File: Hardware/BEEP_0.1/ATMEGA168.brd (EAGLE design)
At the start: 48.8 x 53 mm, 22 parts, among them IC1 ATMEGA48/88/168-AU, Q1 20Mhz

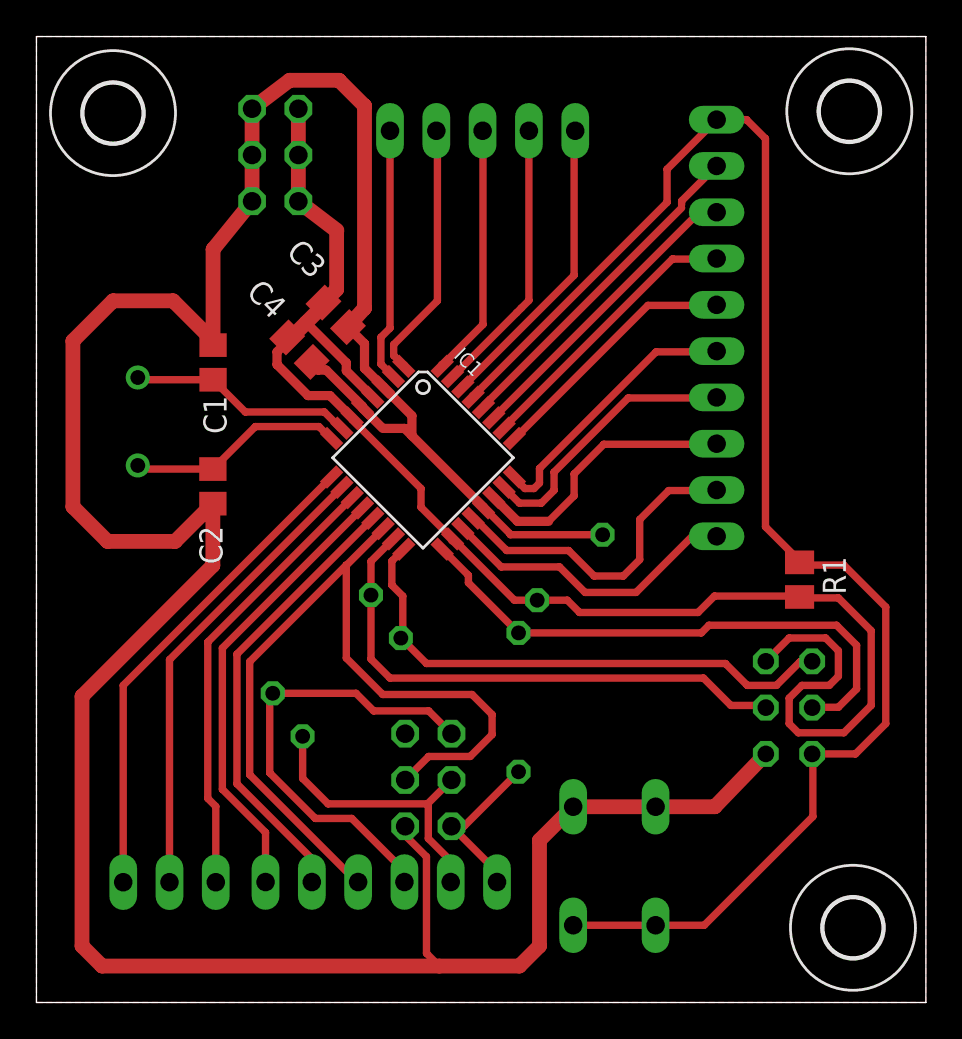
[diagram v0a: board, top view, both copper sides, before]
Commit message: enlarge Clearence to 10mil created some pdf files for the boards
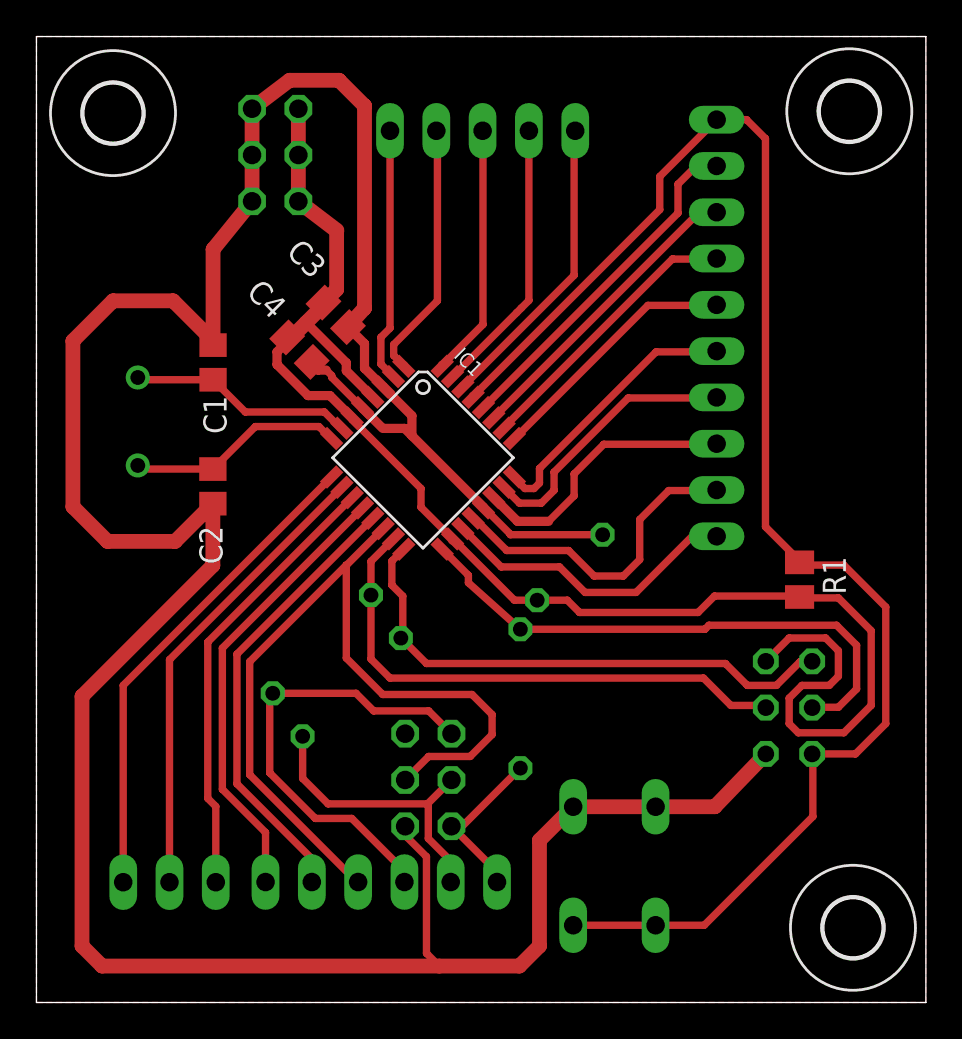
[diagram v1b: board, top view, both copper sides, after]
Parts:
- moved R4 0.22 mm to (26.6, 16.7)
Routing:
- net N$3: track 18.4 -> 19.4 mm
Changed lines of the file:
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@@
 <layers>
 <layer number="1" name="Top" color="4" fill="1" visible="yes" active="yes"/>
-<layer number="16" name="Bottom" color="1" fill="1" visible="yes" active="yes"/>
+<layer number="16" name="Bottom" color="1" fill="1" visible="no" active="yes"/>
 <layer number="17" name="Pads" color="2" fill="1" visible="yes" active="yes"/>
-<layer number="18" name="Vias" color="2" fill="1" visible="yes" active="yes"/>
-<layer number="19" name="Unrouted" color="6" fill="1" visible="yes" active="yes"/>
-<layer number="20" name="Dimension" color="15" fill="1" visible="yes" active="yes"/>
-<layer number="21" name="tPlace" color="7" fill="1" visible="yes" active="yes"/>
-<layer number="22" name="bPlace" color="7" fill="1" visible="yes" active="yes"/>
-<layer number="23" name="tOrigins" color="15" fill="1" visible="yes" active="yes"/>
-<layer number="24" name="bOrigins" color="15" fill="1" visible="yes" active="yes"/>
-<layer number="25" name="tNames" color="7" fill="1" visible="yes" active="yes"/>
-<layer number="26" name="bNames" color="7" fill="1" visible="yes" active="yes"/>
-<layer number="27" name="tValues" color="7" fill="1" visible="yes" active="yes"/>
-<layer number="28" name="bValues" color="7" fill="1" visible="yes" active="yes"/>
+<layer number="18" name="Vias" color="2" fill="1" visible="no" active="yes"/>
+<layer number="19" name="Unrouted" color="6" fill="1" visible="no" active="yes"/>
+<layer number="20" name="Dimension" color="15" fill="1" visible="no" active="yes"/>
+<layer number="21" name="tPlace" color="7" fill="1" visible="no" active="yes"/>
+<layer number="22" name="bPlace" color="7" fill="1" visible="no" active="yes"/>
+<layer number="23" name="tOrigins" color="15" fill="1" visible="no" active="yes"/>
+<layer number="24" name="bOrigins" color="15" fill="1" visible="no" active="yes"/>
+<layer number="25" name="tNames" color="7" fill="1" visible="no" active="yes"/>
+<layer number="26" name="bNames" color="7" fill="1" visible="no" active="yes"/>
+<layer number="27" name="tValues" color="7" fill="1" visible="no" active="yes"/>
+<layer number="28" name="bValues" color="7" fill="1" visible="no" active="yes"/>
 <layer number="29" name="tStop" color="7" fill="3" visible="no" active="yes"/>
 <layer number="30" name="bStop" color="7" fill="6" visible="no" active="yes"/>
@@
 <layer number="37" name="tTest" color="7" fill="1" visible="no" active="yes"/>
 <layer number="38" name="bTest" color="7" fill="1" visible="no" active="yes"/>
-<layer number="39" name="tKeepout" color="4" fill="11" visible="yes" active="yes"/>
-<layer number="40" name="bKeepout" color="1" fill="11" visible="yes" active="yes"/>
-<layer number="41" name="tRestrict" color="4" fill="10" visible="yes" active="yes"/>
-<layer number="42" name="bRestrict" color="1" fill="10" visible="yes" active="yes"/>
-<layer number="43" name="vRestrict" color="2" fill="10" visible="yes" active="yes"/>
+<layer number="39" name="tKeepout" color="4" fill="11" visible="no" active="yes"/>
+<layer number="40" name="bKeepout" color="1" fill="11" visible="no" active="yes"/>
+<layer number="41" name="tRestrict" color="4" fill="10" visible="no" active="yes"/>
+<layer number="42" name="bRestrict" color="1" fill="10" visible="no" active="yes"/>
+<layer number="43" name="vRestrict" color="2" fill="10" visible="no" active="yes"/>
 <layer number="44" name="Drills" color="7" fill="1" visible="no" active="yes"/>
-<layer number="45" name="Holes" color="7" fill="1" visible="yes" active="yes"/>
+<layer number="45" name="Holes" color="7" fill="1" visible="no" active="yes"/>
 <layer number="46" name="Milling" color="3" fill="1" visible="no" active="yes"/>
 <layer number="47" name="Measures" color="7" fill="1" visible="no" active="yes"/>
-<layer number="48" name="Document" color="7" fill="1" visible="yes" active="yes"/>
-<layer number="49" name="Reference" color="7" fill="1" visible="yes" active="yes"/>
+<layer number="48" name="Document" color="7" fill="1" visible="no" active="yes"/>
+<layer number="49" name="Reference" color="7" fill="1" visible="no" active="yes"/>
 <layer number="50" name="dxf" color="7" fill="1" visible="no" active="no"/>
-<layer number="51" name="tDocu" color="7" fill="1" visible="yes" active="yes"/>
-<layer number="52" name="bDocu" color="7" fill="1" visible="yes" active="yes"/>
+<layer number="51" name="tDocu" color="7" fill="1" visible="no" active="yes"/>
+<layer number="52" name="bDocu" color="7" fill="1" visible="no" active="yes"/>
 <layer number="91" name="Nets" color="2" fill="1" visible="no" active="no"/>
 <layer number="92" name="Busses" color="1" fill="1" visible="no" active="no"/>
@@
 </class>
 </classes>
-<designrules name="default">
+<designrules name="default *">
 <description language="de">&lt;b&gt;EAGLE Design Rules&lt;/b&gt;
 &lt;p&gt;
@@
 <param name="mtCopper" value="0.035mm 0.035mm 0.035mm 0.035mm 0.035mm 0.035mm 0.035mm 0.035mm 0.035mm 0.035mm 0.035mm 0.035mm 0.035mm 0.035mm 0.035mm 0.035mm"/>
 <param name="mtIsolate" value="1.5mm 0.15mm 0.2mm 0.15mm 0.2mm 0.15mm 0.2mm 0.15mm 0.2mm 0.15mm 0.2mm 0.15mm 0.2mm 0.15mm 0.2mm"/>
-<param name="mdWireWire" value="8mil"/>
+<param name="mdWireWire" value="10mil"/>
 <param name="mdWirePad" value="8mil"/>
 <param name="mdWireVia" value="8mil"/>
@@
 <attribute name="VALUE" x="20.911578125" y="17.5213125" size="1.27" layer="28" ratio="10" rot="MR315"/>
 </element>
-<element name="R4" library="rcl" package="0207/7" value="1k" x="26.45" y="16.47" rot="MR270"/>
+<element name="R4" library="rcl" package="0207/7" value="1k" x="26.55" y="16.67" rot="MR270"/>
 <element name="SPI" library="pinhead" package="2X03" value="" x="21.5" y="12.21" smashed="yes" rot="MR270">
 <attribute name="NAME" x="18.325" y="13.72" size="1.27" layer="26" ratio="10" rot="MR270"/>
@@
 <wire x1="18" y1="34.8" x2="18" y2="36.149996875" width="0.508" layer="1"/>
 <wire x1="18" y1="36.149996875" x2="17.09175" y2="37.058246875" width="0.508" layer="1"/>
-<wire x1="17.891828125" y1="32.64248125" x2="17.891828125" y2="32.708171875" width="0.508" layer="1"/>
-<wire x1="17.891828125" y1="32.708171875" x2="15.9" y2="34.7" width="0.508" layer="1"/>
 <wire x1="15.9" y1="34.7" x2="15.449996875" y2="34.7" width="0.508" layer="1"/>
 <wire x1="15.449996875" y1="34.7" x2="15.10175" y2="35.148246875" width="0.508" layer="1"/>
@@
 <wire x1="20.3" y1="9.1" x2="20.3" y2="9.6" width="0.4064" layer="1"/>
 <wire x1="20.3" y1="9.6" x2="20.23" y2="9.67" width="0.4064" layer="1"/>
+<wire x1="17.891828125" y1="32.64248125" x2="17.85751875" y2="32.64248125" width="0.4064" layer="1"/>
+<wire x1="17.85751875" y1="32.64248125" x2="16.2" y2="34.3" width="0.4064" layer="1"/>
+<wire x1="16.2" y1="34.3" x2="16.2" y2="34.4" width="0.4064" layer="1"/>
+<wire x1="16.2" y1="34.4" x2="15.9" y2="34.7" width="0.4064" layer="1"/>
 </signal>
 <signal name="VCC">
@@
 <wire x1="40" y1="26.1" x2="40" y2="47.4" width="0.4064" layer="1"/>
 <wire x1="40" y1="47.4" x2="38.96" y2="48.44" width="0.4064" layer="1"/>
-<wire x1="23.96248125" y1="33.26248125" x2="34.6" y2="43.9" width="0.4064" layer="1"/>
-<wire x1="34.6" y1="43.9" x2="34.6" y2="45.72" width="0.4064" layer="1"/>
-<wire x1="34.6" y1="45.72" x2="37.32" y2="48.44" width="0.4064" layer="1"/>
+<wire x1="23.96248125" y1="33.26248125" x2="34.2" y2="43.5" width="0.4064" layer="1"/>
+<wire x1="34.2" y1="43.5" x2="34.2" y2="45.32" width="0.4064" layer="1"/>
+<wire x1="34.2" y1="45.32" x2="37.32" y2="48.44" width="0.4064" layer="1"/>
 <wire x1="37.32" y1="48.44" x2="38.96" y2="48.44" width="0.4064" layer="1"/>
 </signal>
@@
 <wire x1="42.58" y1="16.2" x2="42.56" y2="16.18" width="0.4064" layer="1"/>
 <wire x1="23.7" y1="23.440196875" x2="23.7" y2="23.03" width="0.4064" layer="1"/>
-<wire x1="23.7" y1="23.03" x2="26.45" y2="20.28" width="0.4064" layer="1"/>
-<wire x1="26.45" y1="20.28" x2="36.48" y2="20.28" width="0.4064" layer="1"/>
-<wire x1="36.48" y1="20.28" x2="36.9" y2="20.7" width="0.4064" layer="1"/>
+<wire x1="23.7" y1="23.03" x2="26.55" y2="20.48" width="0.4064" layer="1"/>
+<wire x1="26.55" y1="20.48" x2="36.68" y2="20.48" width="0.4064" layer="1"/>
+<wire x1="36.68" y1="20.48" x2="36.9" y2="20.7" width="0.4064" layer="1"/>
 </signal>
 <signal name="SIN">
@@
 <wire x1="25.27" y1="6.61" x2="25.27" y2="7.17" width="0.4064" layer="1"/>
 <wire x1="25.27" y1="7.17" x2="22.77" y2="9.67" width="0.4064" layer="1"/>
-<wire x1="22.77" y1="9.67" x2="23.46" y2="9.67" width="0.4064" layer="1"/>
-<wire x1="23.46" y1="9.67" x2="26.45" y2="12.66" width="0.4064" layer="1"/>
+<wire x1="22.77" y1="9.67" x2="23.36" y2="9.67" width="0.4064" layer="1"/>
+<wire x1="23.36" y1="9.67" x2="26.55" y2="12.86" width="0.4064" layer="1"/>
 </signal>
 <signal name="SS">
@@
 <wire x1="24.52816875" y1="32.64248125" x2="24.59248125" y2="32.64248125" width="0.4064" layer="1"/>
 <wire x1="24.59248125" y1="32.64248125" x2="24.59248125" y2="32.79248125" width="0.4064" layer="1"/>
-<wire x1="24.59248125" y1="32.79248125" x2="35.4" y2="43.6" width="0.4064" layer="1"/>
-<wire x1="35.4" y1="43.78" x2="35.4" y2="43.98" width="0.4064" layer="1"/>
-<wire x1="35.4" y1="43.98" x2="37.32" y2="45.9" width="0.4064" layer="1"/>
-<wire x1="35.4" y1="43.6" x2="35.4" y2="43.78" width="0" layer="19" extent="1-1"/>
+<wire x1="37.32" y1="45.9" x2="36.2" y2="45.9" width="0.4064" layer="1"/>
+<wire x1="36.2" y1="45.9" x2="35.2" y2="44.9" width="0.4064" layer="1"/>
+<wire x1="35.2" y1="44.9" x2="35.2" y2="43.3143125" width="0.4064" layer="1"/>
+<wire x1="35.2" y1="43.3143125" x2="24.52816875" y2="32.64248125" width="0.4064" layer="1"/>
 </signal>
 <signal name="N$4">

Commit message: Add branding ;) enhance PCBs finish Easy RGB Board add Texas Instruments libray from Element 14 add dxf import ulp for eagle add Script for easy eagle export to pdf for etching minor cleanup
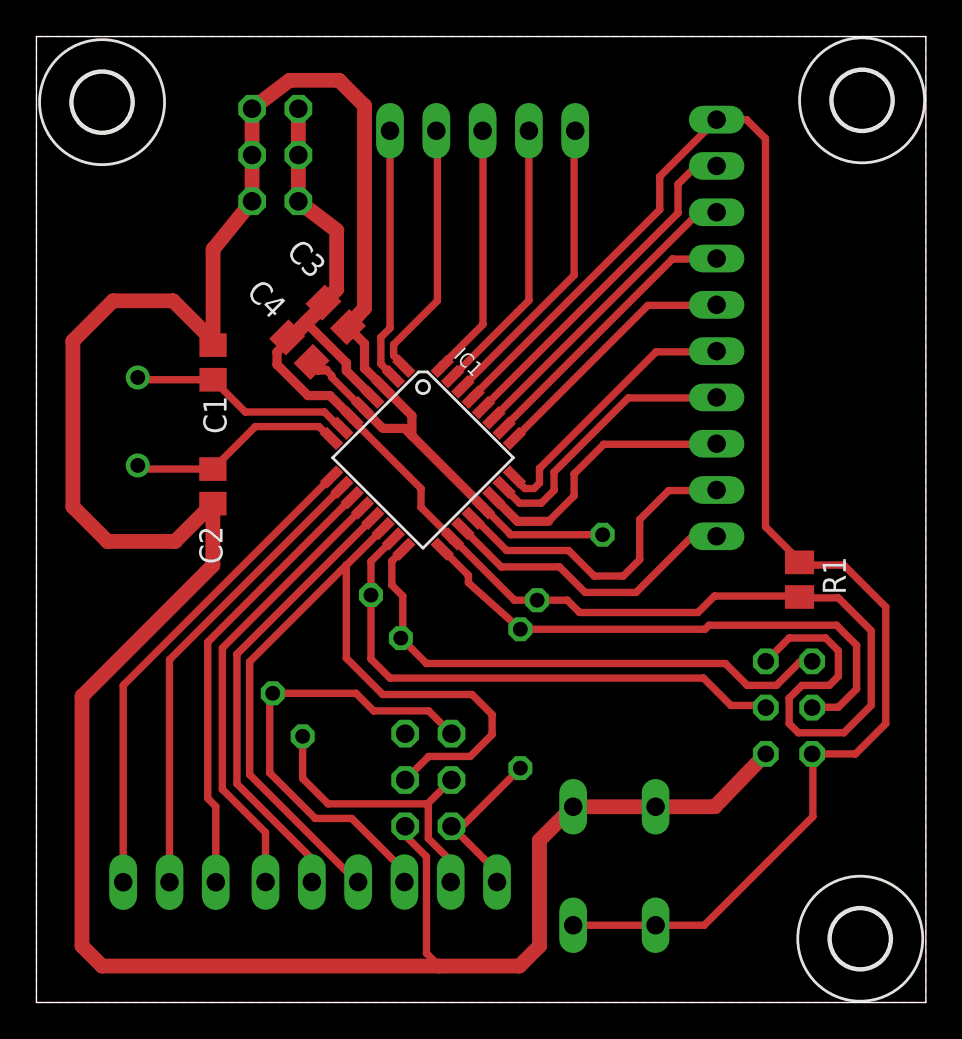
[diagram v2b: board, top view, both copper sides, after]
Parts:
- added U$1: LOGO-COPPER4, Branding:COPPER4
- moved H2 0.92 mm to (45.3, 49.5)
- moved H1 0.85 mm to (3.60, 49.4)
- moved H3 0.72 mm to (45.2, 3.50)
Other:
- board text added: "ATmega168 v0.1.1"
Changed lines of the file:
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@@
 <layers>
 <layer number="1" name="Top" color="4" fill="1" visible="yes" active="yes"/>
-<layer number="16" name="Bottom" color="1" fill="1" visible="no" active="yes"/>
+<layer number="16" name="Bottom" color="1" fill="1" visible="yes" active="yes"/>
 <layer number="17" name="Pads" color="2" fill="1" visible="yes" active="yes"/>
-<layer number="18" name="Vias" color="2" fill="1" visible="no" active="yes"/>
-<layer number="19" name="Unrouted" color="6" fill="1" visible="no" active="yes"/>
-<layer number="20" name="Dimension" color="15" fill="1" visible="no" active="yes"/>
-<layer number="21" name="tPlace" color="7" fill="1" visible="no" active="yes"/>
-<layer number="22" name="bPlace" color="7" fill="1" visible="no" active="yes"/>
-<layer number="23" name="tOrigins" color="15" fill="1" visible="no" active="yes"/>
-<layer number="24" name="bOrigins" color="15" fill="1" visible="no" active="yes"/>
-<layer number="25" name="tNames" color="7" fill="1" visible="no" active="yes"/>
-<layer number="26" name="bNames" color="7" fill="1" visible="no" active="yes"/>
-<layer number="27" name="tValues" color="7" fill="1" visible="no" active="yes"/>
-<layer number="28" name="bValues" color="7" fill="1" visible="no" active="yes"/>
+<layer number="18" name="Vias" color="2" fill="1" visible="yes" active="yes"/>
+<layer number="19" name="Unrouted" color="6" fill="1" visible="yes" active="yes"/>
+<layer number="20" name="Dimension" color="15" fill="1" visible="yes" active="yes"/>
+<layer number="21" name="tPlace" color="7" fill="1" visible="yes" active="yes"/>
+<layer number="22" name="bPlace" color="7" fill="1" visible="yes" active="yes"/>
+<layer number="23" name="tOrigins" color="15" fill="1" visible="yes" active="yes"/>
+<layer number="24" name="bOrigins" color="15" fill="1" visible="yes" active="yes"/>
+<layer number="25" name="tNames" color="7" fill="1" visible="yes" active="yes"/>
+<layer number="26" name="bNames" color="7" fill="1" visible="yes" active="yes"/>
+<layer number="27" name="tValues" color="7" fill="1" visible="yes" active="yes"/>
+<layer number="28" name="bValues" color="7" fill="1" visible="yes" active="yes"/>
 <layer number="29" name="tStop" color="7" fill="3" visible="no" active="yes"/>
 <layer number="30" name="bStop" color="7" fill="6" visible="no" active="yes"/>
@@
 <layer number="37" name="tTest" color="7" fill="1" visible="no" active="yes"/>
 <layer number="38" name="bTest" color="7" fill="1" visible="no" active="yes"/>
-<layer number="39" name="tKeepout" color="4" fill="11" visible="no" active="yes"/>
-<layer number="40" name="bKeepout" color="1" fill="11" visible="no" active="yes"/>
-<layer number="41" name="tRestrict" color="4" fill="10" visible="no" active="yes"/>
-<layer number="42" name="bRestrict" color="1" fill="10" visible="no" active="yes"/>
-<layer number="43" name="vRestrict" color="2" fill="10" visible="no" active="yes"/>
+<layer number="39" name="tKeepout" color="4" fill="11" visible="yes" active="yes"/>
+<layer number="40" name="bKeepout" color="1" fill="11" visible="yes" active="yes"/>
+<layer number="41" name="tRestrict" color="4" fill="10" visible="yes" active="yes"/>
+<layer number="42" name="bRestrict" color="1" fill="10" visible="yes" active="yes"/>
+<layer number="43" name="vRestrict" color="2" fill="10" visible="yes" active="yes"/>
 <layer number="44" name="Drills" color="7" fill="1" visible="no" active="yes"/>
-<layer number="45" name="Holes" color="7" fill="1" visible="no" active="yes"/>
+<layer number="45" name="Holes" color="7" fill="1" visible="yes" active="yes"/>
 <layer number="46" name="Milling" color="3" fill="1" visible="no" active="yes"/>
 <layer number="47" name="Measures" color="7" fill="1" visible="no" active="yes"/>
@@
 <layer number="49" name="Reference" color="7" fill="1" visible="no" active="yes"/>
 <layer number="50" name="dxf" color="7" fill="1" visible="no" active="no"/>
-<layer number="51" name="tDocu" color="7" fill="1" visible="no" active="yes"/>
-<layer number="52" name="bDocu" color="7" fill="1" visible="no" active="yes"/>
+<layer number="51" name="tDocu" color="7" fill="1" visible="yes" active="yes"/>
+<layer number="52" name="bDocu" color="7" fill="1" visible="yes" active="yes"/>
 <layer number="91" name="Nets" color="2" fill="1" visible="no" active="no"/>
 <layer number="92" name="Busses" color="1" fill="1" visible="no" active="no"/>
@@
 <layer number="97" name="Info" color="7" fill="1" visible="no" active="no"/>
 <layer number="98" name="Guide" color="6" fill="1" visible="no" active="no"/>
+<layer number="100" name="tCName" color="7" fill="1" visible="yes" active="yes"/>
+<layer number="101" name="bCName" color="7" fill="1" visible="yes" active="yes"/>
 </layers>
 <board>
@@
 <text x="15.9" y="44" size="1.778" layer="26" rot="MR90">VCC</text>
 <text x="8.4" y="43.9" size="1.778" layer="26" rot="MR90">GND</text>
+<text x="47.6" y="26.1" size="1.778" layer="100" rot="R90">ATmega168
+v0.1.1</text>
+<polygon width="0.4064" layer="41">
+<vertex x="47.8" y="26.1"/>
+<vertex x="42.6" y="26.1"/>
+<vertex x="42.6" y="42.3"/>
+<vertex x="42.6" y="42.4"/>
+<vertex x="44.9" y="44.7"/>
+<vertex x="47.9" y="44.7"/>
+<vertex x="47.9" y="26.1"/>
+</polygon>
 </plain>
 <attributes>
@@
 <attribute name="VALUE" x="17.545" y="50.31" size="1.27" layer="28" rot="MR270"/>
 </element>
-<element name="H1" library="holes" package="3,2" value="" x="4.2" y="48.8"/>
-<element name="H2" library="holes" package="3,2" value="" x="44.6" y="48.9"/>
-<element name="H3" library="holes" package="3,2" value="" x="44.8" y="4.1"/>
+<element name="H1" library="holes" package="3,2" value="" x="3.6" y="49.4"/>
+<element name="H2" library="holes" package="3,2" value="" x="45.3" y="49.5"/>
+<element name="H3" library="holes" package="3,2" value="" x="45.2" y="3.5"/>
+<element name="U$1" library="Branding" package="COPPER4" value="LOGO-COPPER4" x="47.7" y="37.7" rot="R90"/>
 </elements>
 <signals>
@@
 </board>
 </drawing>
+<compatibility>
+<note version="6.3" minversion="6.2.2" severity="warning">
+Since Version 6.2.2 text objects can contain more than one line,
+which will not be processed correctly with this version.
+</note>
+</compatibility>
 </eagle>
